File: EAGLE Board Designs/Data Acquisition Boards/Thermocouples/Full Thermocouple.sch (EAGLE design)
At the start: 32 parts, among them U1 MAX31855K, U2 MAX31855K, U3 MAX31855K, U4 MAX31855K, U5 MAX31855K, U6 MAX31855K, X1 CONNECTOR-4NANO-FIT-VERTICAL-4

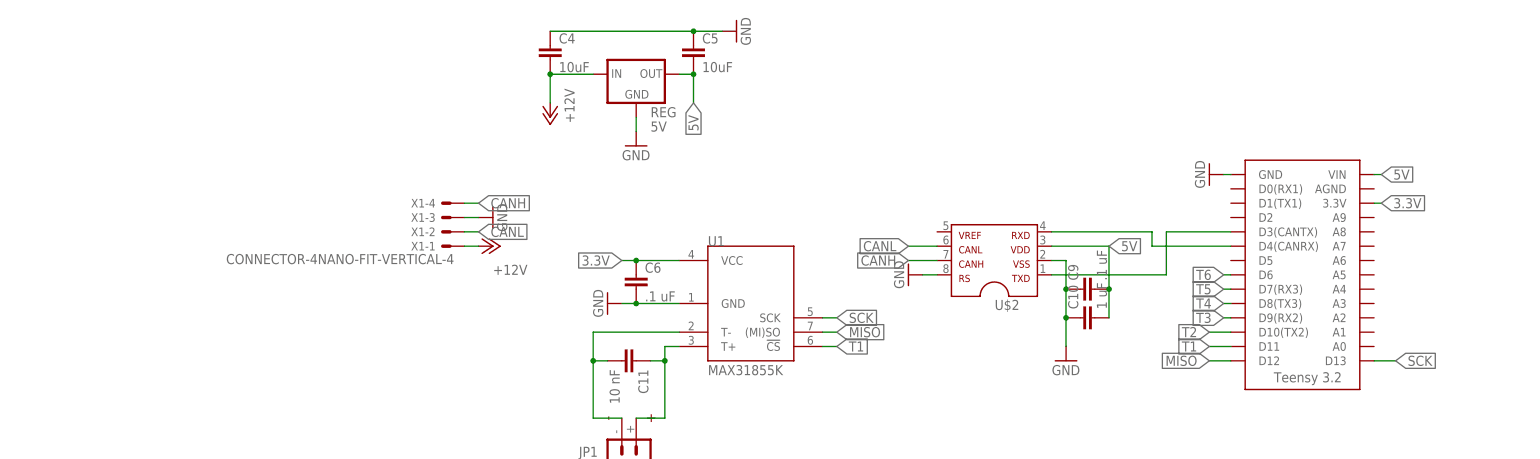
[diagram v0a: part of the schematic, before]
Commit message: Routed Thermocouple Board
Finished routing new thermocouple board
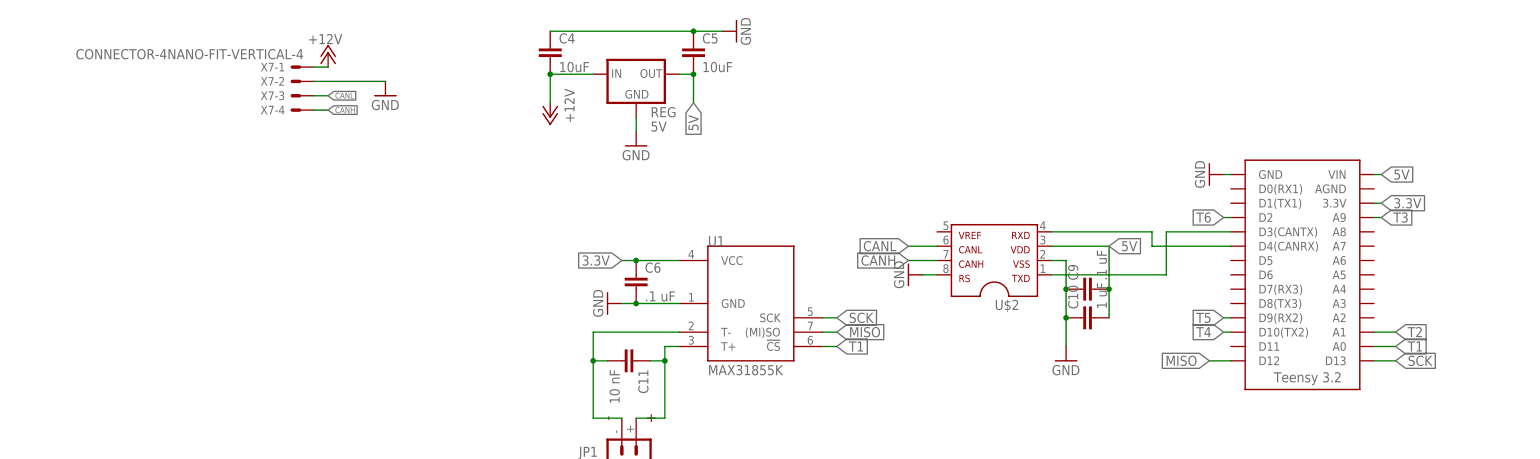
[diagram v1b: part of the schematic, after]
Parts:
- removed X1: CONNECTOR-4NANO-FIT-VERTICAL-4, HyTechDevices:CONNECTOR-4NANO-FIT-VERTICAL-4
- added X7: CONNECTOR-4NANO-FIT-VERTICAL-4, HyTechDevices:CONNECTOR-4NANO-FIT-VERTICAL-4
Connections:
- net +12V: now also X7-1.S; no longer X1-1.S
- net CANH: now also X7-4.S; no longer X1-4.S
- net CANL: now also X7-3.S; no longer X1-2.S
- net GND: now also X7-2.S; no longer X1-3.S
- net T1: now also U$1.A0; no longer U$1.D11
- net T2: now also U$1.A1; no longer U$1.D10(TX2)
- net T3: now also U$1.A9; no longer U$1.D9(RX2)
- net T4: now also U$1.D10(TX2); no longer U$1.D8(TX3)
- net T5: now also U$1.D9(RX2); no longer U$1.D7(RX3)
- net T6: now also U$1.D2; no longer U$1.D6
